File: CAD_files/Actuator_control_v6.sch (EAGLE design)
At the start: 35 parts, among them Y1 16MHz

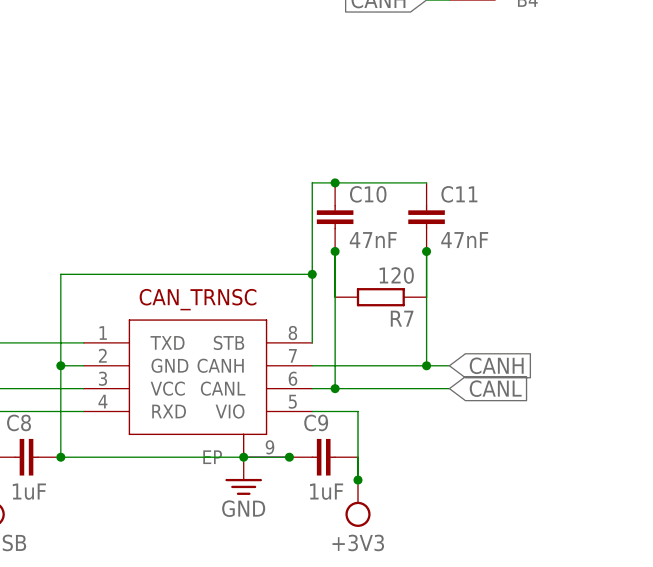
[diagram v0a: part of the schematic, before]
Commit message: Resolved issue #9
Removed CAN lines capacitors and added info regarding terminating resistors
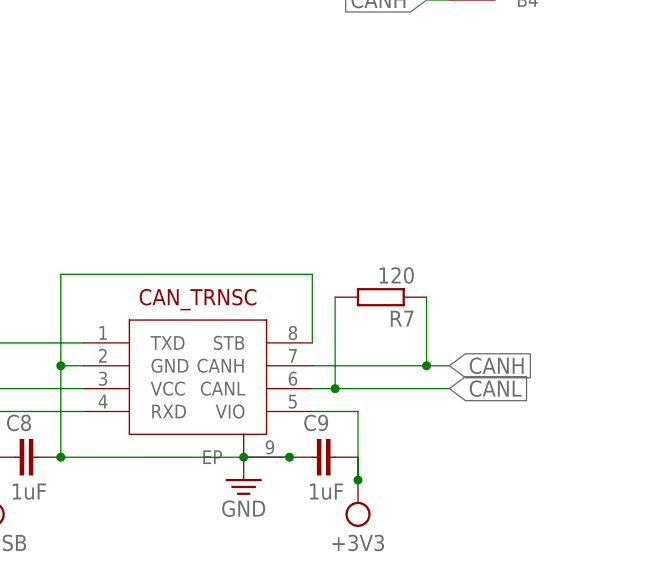
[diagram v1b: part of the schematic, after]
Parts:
- removed C10, C11: 47nF, resistor:C-EUC0402
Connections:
- net CANH: no longer C11.2
- net CANL: no longer C10.2
- net GND: no longer C10.1, C11.1
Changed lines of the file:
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@@
 <part name="C9" library="resistor" library_urn="urn:adsk.eagle:library:348" deviceset="C-EU" device="C0402" package3d_urn="urn:adsk.eagle:package:23626/2" value="1uF"/>
 <part name="R7" library="resistor" library_urn="urn:adsk.eagle:library:348" deviceset="R-EU_" device="R0402" package3d_urn="urn:adsk.eagle:package:26058/2" value="120"/>
-<part name="C10" library="resistor" library_urn="urn:adsk.eagle:library:348" deviceset="C-EU" device="C0402" package3d_urn="urn:adsk.eagle:package:23626/2" value="47nF"/>
-<part name="C11" library="resistor" library_urn="urn:adsk.eagle:library:348" deviceset="C-EU" device="C0402" package3d_urn="urn:adsk.eagle:package:23626/2" value="47nF"/>
 <part name="SUPPLY19" library="Power_Symbols" library_urn="urn:adsk.eagle:library:16502351" deviceset="VCC-CIRCLE" device="" value="+3V3"/>
 <part name="SUPPLY22" library="Power_Symbols" library_urn="urn:adsk.eagle:library:16502351" deviceset="GND-EARTH" device="" value="GND"/>
@@
 <attribute name="VALUE" x="252.73" y="33.782" size="1.778" layer="96" rot="R180"/>
 </instance>
-<instance part="C10" gate="G$1" x="243.84" y="40.64" smashed="yes">
-<attribute name="NAME" x="245.364" y="41.021" size="1.778" layer="95"/>
-<attribute name="VALUE" x="245.364" y="35.941" size="1.778" layer="96"/>
-</instance>
-<instance part="C11" gate="G$1" x="254" y="40.64" smashed="yes">
-<attribute name="NAME" x="255.524" y="41.021" size="1.778" layer="95"/>
-<attribute name="VALUE" x="255.524" y="35.941" size="1.778" layer="96"/>
-</instance>
 <instance part="SUPPLY19" gate="G$1" x="12.7" y="33.02" smashed="yes">
 <attribute name="VALUE" x="12.7" y="37.465" size="1.778" layer="96" align="center"/>
@@
 <wire x1="241.3" y1="33.02" x2="213.36" y2="33.02" width="0.1524" layer="91"/>
 <wire x1="213.36" y1="33.02" x2="213.36" y2="22.86" width="0.1524" layer="91"/>
-<pinref part="C11" gate="G$1" pin="1"/>
-<wire x1="254" y1="43.18" x2="243.84" y2="43.18" width="0.1524" layer="91"/>
-<pinref part="C10" gate="G$1" pin="1"/>
-<wire x1="243.84" y1="43.18" x2="241.3" y2="43.18" width="0.1524" layer="91"/>
-<wire x1="241.3" y1="43.18" x2="241.3" y2="33.02" width="0.1524" layer="91"/>
 <junction x="213.36" y="22.86"/>
 <junction x="213.36" y="12.7"/>
 <junction x="233.68" y="12.7"/>
 <junction x="238.76" y="12.7"/>
-<junction x="241.3" y="33.02"/>
-<junction x="243.84" y="43.18"/>
 </segment>
 <segment>
@@
 <pinref part="R7" gate="G$1" pin="1"/>
 <wire x1="254" y1="22.86" x2="256.54" y2="22.86" width="0.1524" layer="91"/>
-<wire x1="254" y1="35.56" x2="254" y2="22.86" width="0.1524" layer="91"/>
-<pinref part="C11" gate="G$1" pin="2"/>
-<wire x1="254" y1="35.56" x2="254" y2="30.48" width="0.1524" layer="91"/>
+<wire x1="254" y1="30.48" x2="254" y2="22.86" width="0.1524" layer="91"/>
 <junction x="254" y="22.86"/>
-<junction x="254" y="35.56"/>
 </segment>
 <segment>
@@
 <pinref part="R7" gate="G$1" pin="2"/>
 <wire x1="243.84" y1="20.32" x2="256.54" y2="20.32" width="0.1524" layer="91"/>
-<wire x1="243.84" y1="35.56" x2="243.84" y2="20.32" width="0.1524" layer="91"/>
-<pinref part="C10" gate="G$1" pin="2"/>
-<wire x1="243.84" y1="35.56" x2="243.84" y2="30.48" width="0.1524" layer="91"/>
+<wire x1="243.84" y1="30.48" x2="243.84" y2="20.32" width="0.1524" layer="91"/>
 <junction x="243.84" y="20.32"/>
-<junction x="243.84" y="35.56"/>
-</segment>
-<segment>
+</segment>
+<segment>
